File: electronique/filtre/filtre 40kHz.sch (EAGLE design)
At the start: 47 parts, among them IC1 TL084P, IC2 TL084P

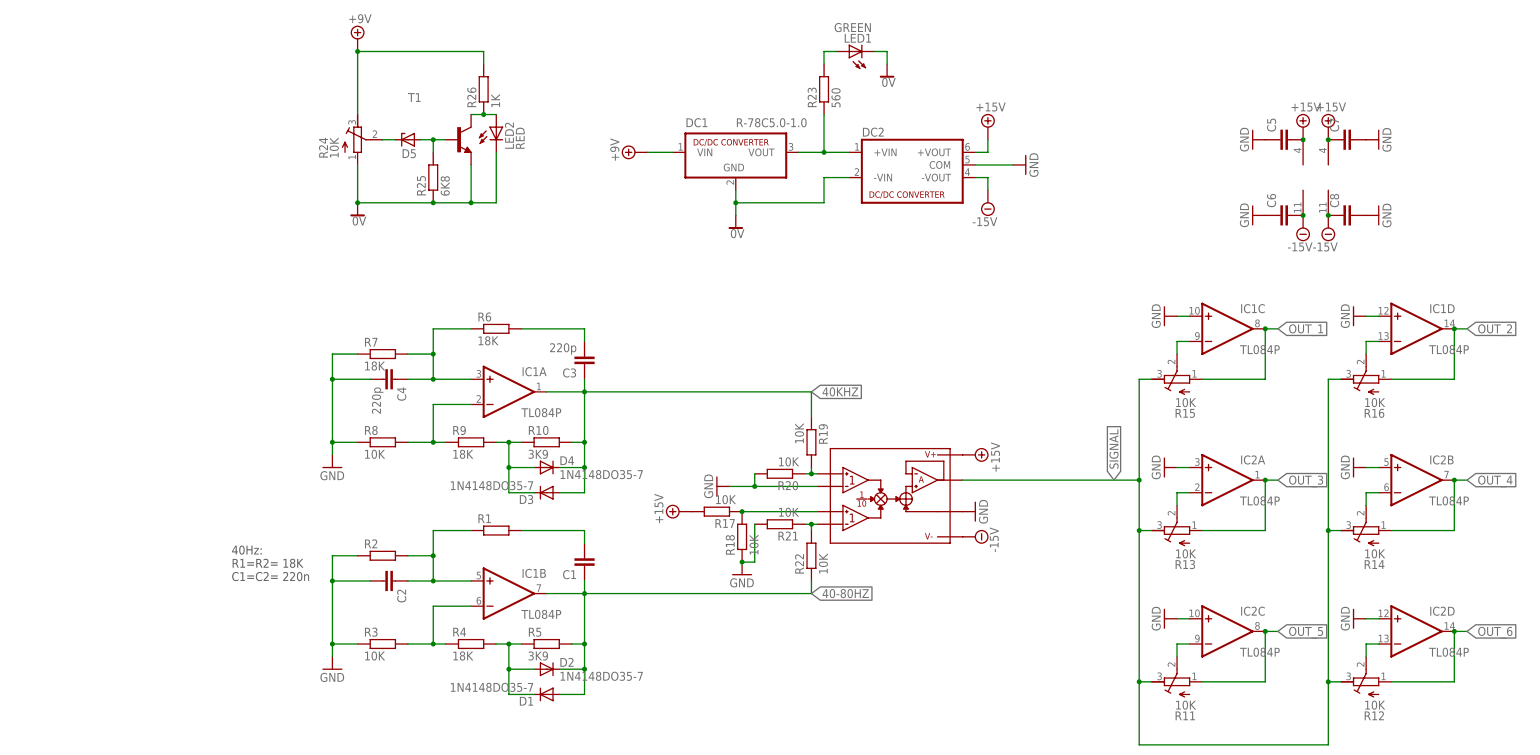
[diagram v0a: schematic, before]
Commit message: circuit balise emission + filtre 80Hz
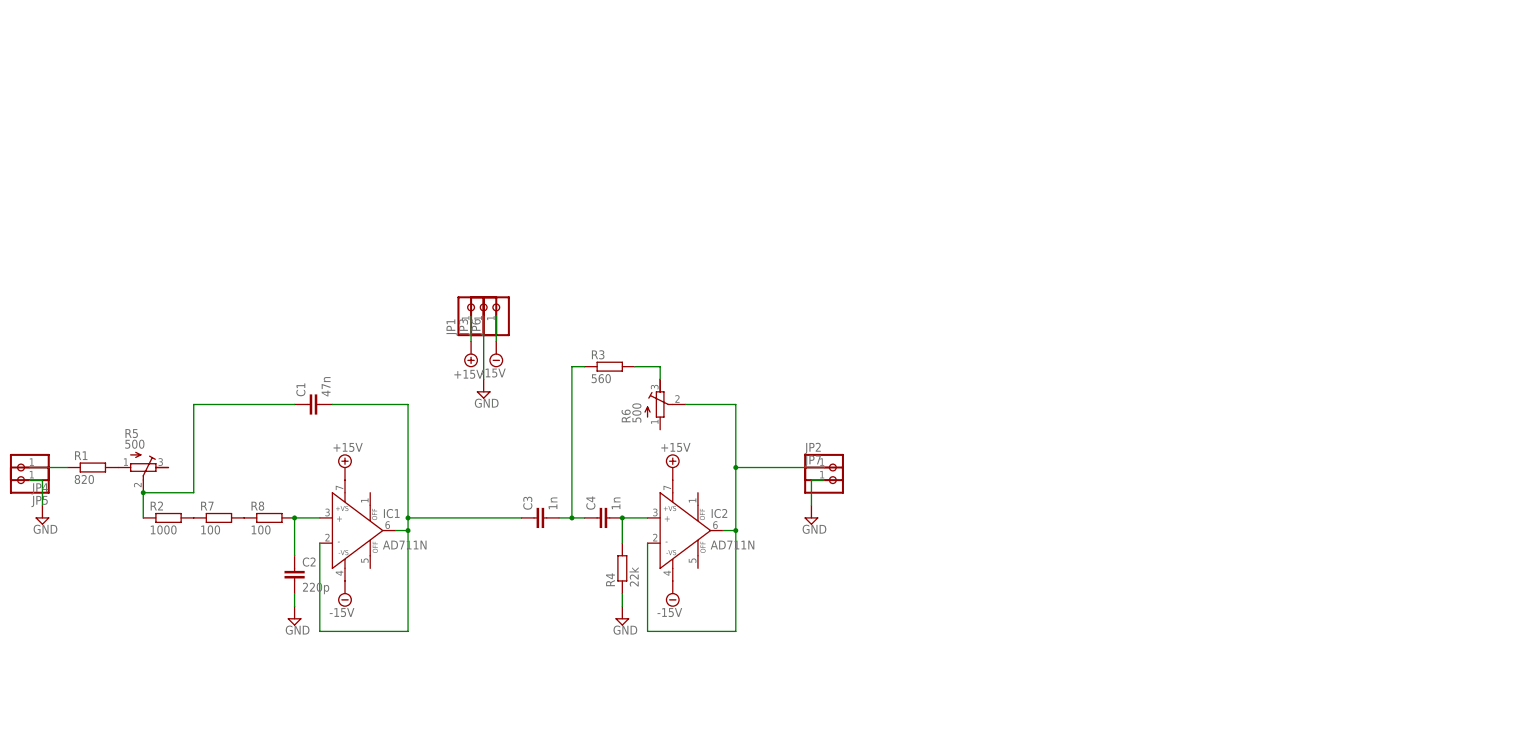
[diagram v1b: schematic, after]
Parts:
- removed C5, C6, C7, C8: (no value), resistor:C-EU050-024X044
- removed D1, D2, D3, D4: 1N4148DO35-7, diode:1N4148DO35-7
- removed D5: (no value), diode:ZENER-DIODEZD-2.5
- removed DC1: R-78C5.0-1.0, dc-dc-converter:R-78C5.0-1.0
- removed DC2: (no value), dc-dc-converter:NMA
- removed LED1: GREEN, led:LEDB155
- removed LED2: RED, led:LEDB155
- removed R10: 3K9, resistor:R-EU_0204/7
- removed R11, R12, R13, R14, R15, R16, R24: 10K, resistor:R-TRIMM3339P
- removed R17, R18, R19, R20, R21, R22: 10K, resistor:R-EU_0204/7
- removed R23: 560, resistor:R-EU_0204/7
- removed R25: 6K8, resistor:R-EU_0204/7
- removed R26: 1K, resistor:R-EU_0204/7
- removed R9: 18K, resistor:R-EU_0204/7
- removed T1: (no value), transistor:2N5400-NPN-TO92-CBE
- removed U$1: AD633JN, analog-devices:AD633JN
- added JP1, JP2, JP3, JP4, JP5, JP6, JP7: (no value), pinhead:PINHD-1X1
- C1: value (none) -> 47n; device resistor:C-EU075-032X103 -> resistor:C-EU050-024X044
- C2: value (none) -> 220p; device resistor:C-EU075-032X103 -> resistor:C-EU050-024X044
- C3: value 220p -> 1n
- C4: value 220p -> 1n; device resistor:C-EU075-032X103 -> resistor:C-EU050-024X044
- IC1, IC2: value TL084P -> AD711N; device linear:TL084P -> analog-devices:AD711N
- R1: value (none) -> 820
- R2: value (none) -> 1000
- R3: value 10K -> 560
- R4: value 18K -> 22k
- R5: value 3K9 -> 500; device resistor:R-EU_0204/7 -> resistor:R-TRIMM3339P
- R6: value 18K -> 500; device resistor:R-EU_0204/7 -> resistor:R-TRIMM3339P
- R7: value 18K -> 100; device resistor:R-EU_0204/7 -> resistor:R-EU_0207/2V
- R8: value 10K -> 100; device resistor:R-EU_0204/7 -> resistor:R-EU_0207/2V
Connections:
- removed net +9V: DC1.VIN, R24.A, R26.2
- removed net 0V: DC1.GND, DC2.-VIN, LED1.C, LED2.C, R24.E, R25.1, T1.E
- removed net 40-80HZ: C1.1, D1.A, D2.C, IC1B.OUT, R22.1, R5.2
- removed net 40KHZ: C3.1, D3.A, D4.C, IC1A.OUT, R10.2, R19.1
- removed net N$12: IC2D.-IN, R12.S
- removed net N$13: R19.2, R20.1, U$1.X1
- removed net N$14: LED1.A, R23.2
- removed net N$15: IC2A.-IN, R13.S
- removed net N$16: R21.1, R22.2, U$1.Y2
- removed net N$17: D5.C, R24.S
- removed net N$18: IC2B.-IN, R14.S
- removed net N$19: D5.A, R25.2, T1.B
- removed net N$21: IC1C.-IN, R15.S
- removed net N$22: LED2.A, R26.1, T1.C
- removed net N$24: IC1D.-IN, R16.S
- removed net OUT_1: IC1C.OUT, R15.E
- removed net OUT_2: IC1D.OUT, R16.E
- removed net OUT_3: IC2A.OUT, R13.E
- removed net OUT_4: IC2B.OUT, R14.E
- removed net OUT_5: IC2C.OUT, R11.E
- removed net OUT_6: IC2D.OUT, R12.E
- removed net SIGNAL: R11.A, R12.A, R13.A, R14.A, R15.A, R16.A, U$1.W
- net +15V: now also IC1.+VS, IC2.+VS, JP1.1; no longer C5.2, C7.1, DC2.+VOUT, IC1P.V+, IC2P.V+, R17.2, U$1.+V
- net -15V: now also IC1.-VS, IC2.-VS, JP6.1; no longer C6.2, C8.1, DC2.-VOUT, IC1P.V-, IC2P.V-, U$1.-V
- net GND: now also JP3.1, JP5.1, JP7.1, R4.1; no longer C4.2, C5.1, C6.1, C7.2, C8.2, DC2.COM, IC1C.+IN, IC1D.+IN, IC2A.+IN, IC2B.+IN, IC2C.+IN, IC2D.+IN, R18.1, R2.1, R20.2, R21.2, R3.1, R7.1, R8.1, U$1.X2, U$1.Z
- net N$1: now also C2.1, IC1.IN+, R8.2; no longer IC1B.-IN, R3.2, R4.1
- net N$10: now also R3.2, R6.A; no longer C4.1, IC1A.+IN, R6.1, R7.2
- net N$11: now also JP4.1, R1.1; no longer DC1.VOUT, DC2.+VIN, R23.1
- net N$2: now also R2.2, R7.1; no longer D1.C, D2.A, R4.2, R5.1
- net N$3: now also R7.2, R8.1; no longer IC2C.-IN, R11.S
- net N$4: now also R5.E; no longer C1.2
- net N$5: now also C1.1, R2.1, R5.S; no longer C2.1, IC1B.+IN, R1.1, R2.2
- net N$6: now also C1.2, C3.1, IC1.IN-, IC1.OUT; no longer IC1A.-IN, R8.2, R9.1
- net N$7: now also C3.2, C4.1, R3.1; no longer D3.C, D4.A, R10.1, R9.2
- net N$8: now also C4.2, IC2.IN+, R4.2; no longer R17.1, R18.2, U$1.Y1
- net N$9: now also IC2.IN-, IC2.OUT, JP2.1, R6.S; no longer C3.2, R6.2
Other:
- note removed: "40Hz: R1=R2= 18K C1=C2= 220n"
- moved on the sheet: C1, C2, C3, C4, R1, R2, R3, R4, R7, R8
